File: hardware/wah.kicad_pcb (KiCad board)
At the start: 4 copper layers, 99.1 x 54.5 mm, 34 parts, among them J1 Barrel_Jack_Switch, J2 In, J3 Out, SW1 SW_Push_3PDT, U1 TL072, U2 L78L05_TO92

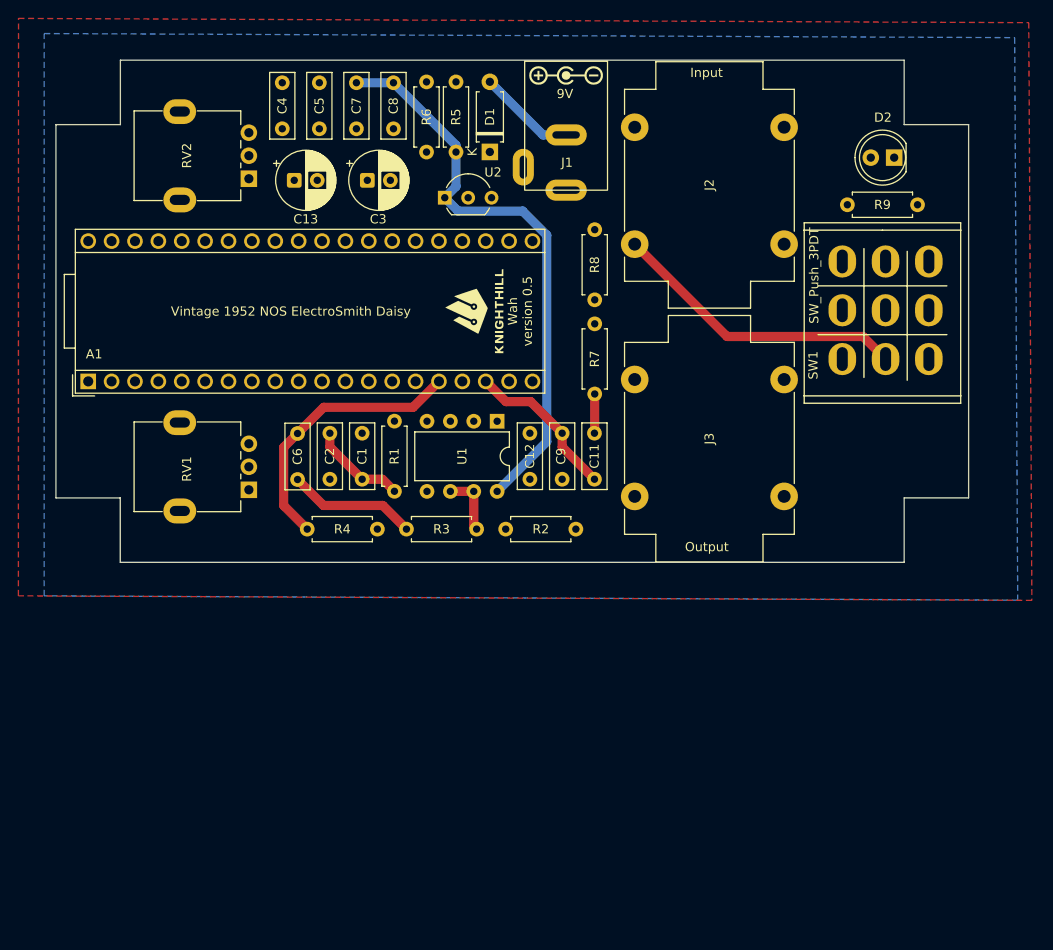
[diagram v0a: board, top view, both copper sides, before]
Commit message: fix footprints
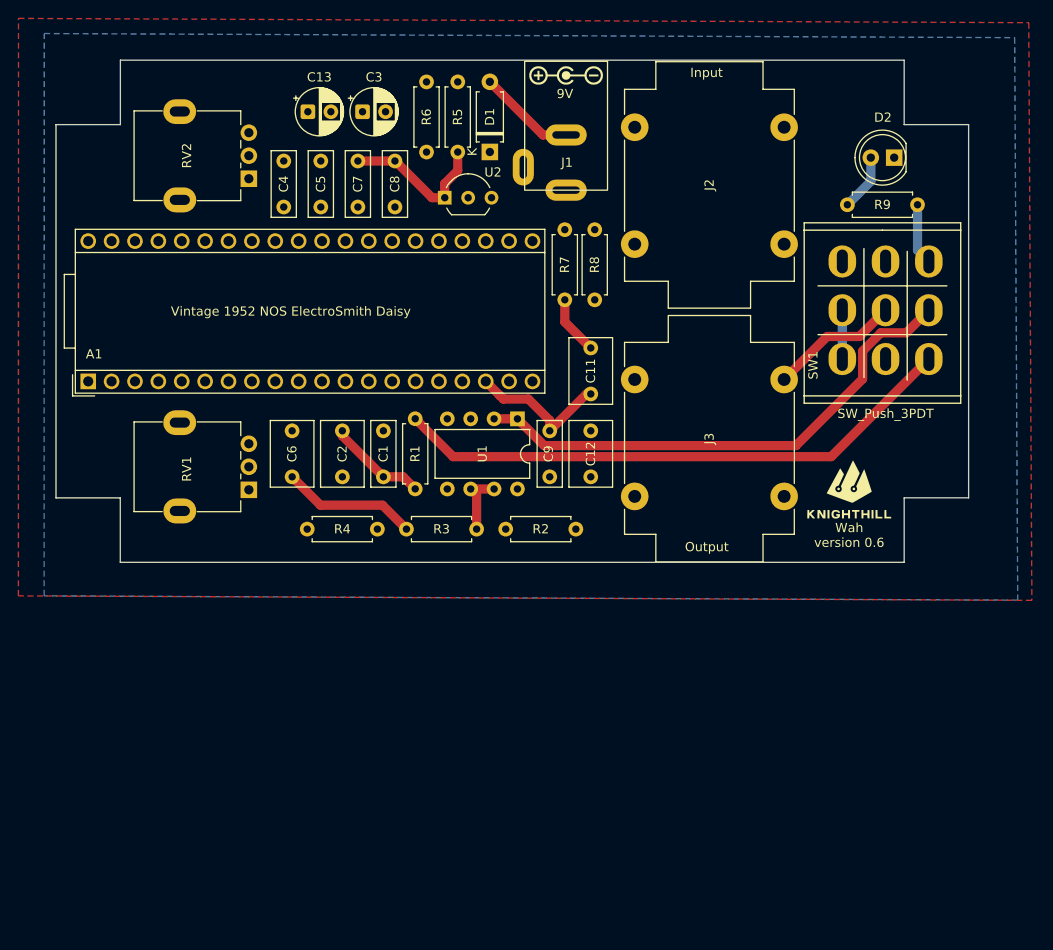
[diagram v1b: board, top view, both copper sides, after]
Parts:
- C11, C12, C2, C6: footprint Capacitor_THT:C_Rect_L7.0mm_W2.5mm_P5.00mm -> Capacitor_THT:C_Rect_L7.0mm_W4.5mm_P5.00mm
- C13, C3: footprint Capacitor_THT:CP_Radial_D6.3mm_P2.50mm -> Capacitor_THT:CP_Radial_D5.0mm_P2.50mm
- moved G*** 44.5 mm to (128.5, 80.7), turned to 0 degrees
- moved R7 10.7 mm to (97.7, 59.2)
- moved C11 9.27 mm to (100.5, 69.4)
- moved C4 8.50 mm to (67.2, 49.1)
- moved C5 8.50 mm to (71.2, 49.1)
- moved C7 8.50 mm to (75.2, 44.1)
- moved C8 8.50 mm to (79.2, 44.1)
- moved C13 7.60 mm to (69.8, 38.8)
- moved C3 7.47 mm to (75.7, 38.8)
- moved C12 6.62 mm to (100.5, 73.4)
- moved C1 2.32 mm to (78.0, 78.4)
- moved R1 2.27 mm to (81.4, 72.1)
- moved U1 2.22 mm to (92.5, 72.1)
- moved C2 1.38 mm to (73.5, 73.4)
- moved C9 1.37 mm to (96.1, 73.4)
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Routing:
- net Net-(U1A-+): track 26.7 -> 39.1 mm
- net Net-(U1C-V+): track 62.7 -> 58.3 mm
- net Net-(U1B-+): track 24.0 -> 21.3 mm
- net /FX_IN: track 64.5 -> 61.9 mm
- net Net-(C11-Pad2): track 4.27 -> 6.40 mm
- net /POT1: track 38.2 -> 36.7 mm
- net /AUDIO_OUT: track 17.1 -> 16.0 mm
- net /AUDIO_IN: track 29.8 -> 30.8 mm
- net Net-(C6-Pad1): track 14.1 -> 14.8 mm
- net /FX_OUT: track 56.9 -> 56.3 mm
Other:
- board text added: "Wah version 0.6"
- board text removed: "Wah version 0.5"

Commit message: rearrange pcb
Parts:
- removed C4, C5: 100n, Capacitor_THT:C_Rect_L7.0mm_W2.5mm_P5.00mm
- moved C7 46.2 mm to (96.4, 85.2), turned to 0 degrees
- moved C8 41.3 mm to (96.4, 81.6), turned to 0 degrees
- moved R2 14.4 mm to (84.6, 85.6)
- moved R3 14.0 mm to (74.2, 85.6)
- moved R1 10.6 mm to (84.6, 82.2), turned to 180 degrees
- moved C13 10.2 mm to (76.5, 46.5)
- moved R4 3.71 mm to (66.5, 82.2)
- moved U1 2.80 mm to (89.8, 71.6)
- moved C1 0.97 mm to (78.4, 77.6)
- moved C2 0.88 mm to (73.7, 72.6)
- moved C6 0.88 mm to (67.9, 77.6)
- moved C3 0.85 mm to (76.5, 39.0)
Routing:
- net Net-(U1B--): track 7.17 -> 15.8 mm
- net Net-(C6-Pad1): track 14.8 -> 9.25 mm
- net Net-(U1B-+): track 21.3 -> 17.7 mm
- net /FX_OUT: track 56.3 -> 59.3 mm
- net Net-(U1A-+): track 39.1 -> 42.1 mm
- net /AUDIO_IN: track 30.8 -> 28.8 mm
- net /FX_IN: track 61.9 -> 60.3 mm
- net Net-(C1-Pad1): track 10.8 -> 12.2 mm
- net /AUDIO_OUT: track 16.0 -> 15.3 mm
- net Net-(U1C-V+): track 58.3 -> 58.9 mm

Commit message: rename resources
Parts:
- renumbered C12 to C10, C7 to C4, C6 to C5, C8 to C6, C13 to C7, C9 to C8, C11 to C9
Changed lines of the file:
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@@
 	(net 38 "Net-(C1-Pad1)")
 	(net 39 "Net-(U1B-+)")
-	(net 40 "Net-(C6-Pad1)")
+	(net 40 "Net-(C5-Pad1)")
 	(net 41 "unconnected-(A1-ADC_3-Pad25)")
 	(net 42 "Net-(U1C-V+)")
-	(net 43 "Net-(C11-Pad2)")
+	(net 43 "Net-(C9-Pad2)")
 	(net 44 "unconnected-(A1-USB_D_--Pad36)")
 	(net 45 "Net-(D1-A)")
@@
 		(descr "C, Rect series, Radial, pin pitch=5.00mm, length*width=7*4.5mm^2, Capacitor")
 		(tags "C Rect series Radial pin pitch 5.00mm length 7mm width 4.5mm Capacitor")
-		(property "Reference" "C11"
+		(property "Reference" "C9"
 			(at 2.5 0 90)
 			(layer "F.SilkS")
@@
 			(layers "*.Cu" "*.Mask")
 			(remove_unused_layers no)
-			(net 43 "Net-(C11-Pad2)")
+			(net 43 "Net-(C9-Pad2)")
 			(pintype "passive")
 		)
@@
 		(descr "C, Rect series, Radial, pin pitch=5.00mm, length*width=7*4.5mm^2, Capacitor")
 		(tags "C Rect series Radial pin pitch 5.00mm length 7mm width 4.5mm Capacitor")
-		(property "Reference" "C6"
+		(property "Reference" "C5"
 			(at 2.5 0 90)
 			(layer "F.SilkS")
@@
 			(layers "*.Cu" "*.Mask")
 			(remove_unused_layers no)
-			(net 40 "Net-(C6-Pad1)")
+			(net 40 "Net-(C5-Pad1)")
 			(pintype "passive")
 		)
@@
 		(descr "CP, Radial series, Radial, pin pitch=2.50mm, diameter=5mm, height=7mm, Electrolytic Capacitor")
 		(tags "CP Radial series Radial pin pitch 2.50mm diameter 5mm height 7mm Electrolytic Capacitor")
-		(property "Reference" "C13"
+		(property "Reference" "C7"
 			(at 1.25 -3.75 0)
 			(layer "F.SilkS")
@@
 		(descr "C, Rect series, Radial, pin pitch=5.00mm, length*width=7*2.5mm^2, Capacitor")
 		(tags "C Rect series Radial pin pitch 5.00mm length 7mm width 2.5mm Capacitor")
-		(property "Reference" "C8"
+		(property "Reference" "C6"
 			(at 2.5 0 0)
 			(layer "F.SilkS")
@@
 			(layers "*.Cu" "*.Mask")
 			(remove_unused_layers no)
-			(net 43 "Net-(C11-Pad2)")
+			(net 43 "Net-(C9-Pad2)")
 			(pintype "passive")
 		)
@@
 			(layers "*.Cu" "*.Mask")
 			(remove_unused_layers no)
-			(net 40 "Net-(C6-Pad1)")
+			(net 40 "Net-(C5-Pad1)")
 			(pintype "passive")
 		)
@@
 		(descr "C, Rect series, Radial, pin pitch=5.00mm, length*width=7*2.5mm^2, Capacitor")
 		(tags "C Rect series Radial pin pitch 5.00mm length 7mm width 2.5mm Capacitor")
-		(property "Reference" "C7"
+		(property "Reference" "C4"
 			(at 2.5 0 0)
 			(layer "F.SilkS")
@@
 		(descr "C, Rect series, Radial, pin pitch=5.00mm, length*width=7*2.5mm^2, Capacitor")
 		(tags "C Rect series Radial pin pitch 5.00mm length 7mm width 2.5mm Capacitor")
-		(property "Reference" "C9"
+		(property "Reference" "C8"
 			(at 2.5 0.125 90)
 			(layer "F.SilkS")
@@
 		(descr "C, Rect series, Radial, pin pitch=5.00mm, length*width=7*4.5mm^2, Capacitor")
 		(tags "C Rect series Radial pin pitch 5.00mm length 7mm width 4.5mm Capacitor")
-		(property "Reference" "C12"
+		(property "Reference" "C10"
 			(at 2.5 0 270)
 			(layer "F.SilkS")

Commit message: pcb
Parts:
- added H1: MountingHole_Pad, MountingHole:MountingHole_3.2mm_M3_Pad, F.Cu at (77.5, 45.9)
- added H2: MountingHole_Pad, MountingHole:MountingHole_3.2mm_M3_Pad, F.Cu at (59.8, 102.8)
- added J4: Conn_01x08_Pin, Connector_PinHeader_2.54mm:PinHeader_1x08_P2.54mm_Vertical, F.Cu at (68.6, 36.0)
- added RV3: 10k, Potentiometer_THT:Potentiometer_Runtron_RM-065_Vertical, F.Cu at (65.5, 92.4)
- added RV4: 10k, Potentiometer_THT:Potentiometer_Runtron_RM-065_Vertical, F.Cu at (56.6, 92.4)
- added SW2: SW_DIP_x04, Button_Switch_THT:SW_DIP_SPSTx04_Slide_9.78x12.34mm_W7.62mm_P2.54mm, F.Cu at (52.6, 87.9)
- RV1, RV2: footprint CustomFootprints:Potentiometer_uxcel_9mm_Single_Vertical -> Potentiometer_THT:Potentiometer_Runtron_RM-065_Vertical
- moved D2 90.3 mm to (78.7, 115.6)
- moved R9 87.0 mm to (72.0, 107.8), turned to -90 degrees
- moved G*** 85.1 mm to (49.4, 112.2)
- moved C3 82.0 mm to (106.4, 115.3)
- moved C7 72.7 mm to (99.9, 115.3)
- moved J3 63.7 mm to (59.6, 53.0), turned to 180 degrees
- moved R8 55.9 mm to (108.8, 107.0), turned to 180 degrees
- moved U2 53.3 mm to (102.5, 98.3)
- moved R5 52.4 mm to (101.2, 93.3), turned to 0 degrees
- moved R6 49.9 mm to (101.2, 89.5), turned to 0 degrees
- moved C9 48.8 mm to (88.8, 116.8), turned to 0 degrees
- moved R7 44.9 mm to (108.8, 102.7), turned to 180 degrees
- moved D1 44.0 mm to (101.2, 85.5), turned to 0 degrees
- moved RV2 38.4 mm to (56.6, 83.8), turned to 90 degrees
- moved C10 38.3 mm to (93.8, 111.2), turned to 180 degrees
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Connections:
- net Net-(J2-PadT) renamed /J_IN
- net Net-(J3-PadT) renamed /J_OUT
- A1 pad 22: unconnected-(A1-ADC_0-Pad22) -> /POT1
- A1 pad 24: /POT1 -> /POT3
- A1 pad 25: unconnected-(A1-ADC_3-Pad25) -> /POT4
- A1 pad 27: unconnected-(A1-ADC_5-Pad27) -> /SW1
- A1 pad 28: unconnected-(A1-ADC_6-Pad28) -> /SW2
- A1 pad 29: unconnected-(A1-DAC_OUT2-Pad29) -> /SW3
- A1 pad 30: unconnected-(A1-DAC_OUT1-Pad30) -> /SW4
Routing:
- net Net-(U1C-V+): track 58.9 -> 0.00 mm
- net Net-(U1A-+): track 42.1 -> 0.00 mm
- net /POT1: track 36.7 -> 0.00 mm
- net /POT2: track 29.6 -> 0.00 mm
- net /AUDIO_IN: track 28.8 -> 0.00 mm
- net /FX_OUT: track 59.3 -> 82.4 mm
- net /FX_IN: track 60.3 -> 78.5 mm
- net Net-(U1B-+): track 17.7 -> 0.00 mm
- net Net-(U1B--): track 15.8 -> 0.00 mm
- net /AUDIO_OUT: track 15.3 -> 0.00 mm
- net Net-(C1-Pad1): track 12.2 -> 0.00 mm
- net Net-(D1-A): track 10.7 -> 0.00 mm
- net /J_OUT: track 14.1 -> 23.9 mm
- net Net-(C5-Pad1): track 9.25 -> 0.00 mm
- net /J_IN: track 32.4 -> 24.8 mm
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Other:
- board size 99.1 x 54.5 mm -> 70 x 87 mm
- board text added: "DryBaby Wah version 0.6"
- board text removed: "Wah version 0.6"

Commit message: pcb changes
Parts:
- removed D2: LED, LED_THT:LED_D5.0mm
- removed R9: R, Resistor_THT:R_Axial_DIN0207_L6.3mm_D2.5mm_P7.62mm_Horizontal
- removed SW1: SW_Push_3PDT, CustomFootprints:Switches_Stomp_Switch_3PDT
- added D3: LED, LED_THT:LED_D5.0mm, F.Cu at (76.2, 41.6)
- added J5: Conn_01x08_Pin, Connector_PinHeader_2.54mm:PinHeader_1x08_P2.54mm_Vertical, F.Cu at (118.7, 93.6)
- added R10: R, Resistor_THT:R_Axial_DIN0207_L6.3mm_D2.5mm_P7.62mm_Horizontal, F.Cu at (83.9, 39.5)
- added SW3: SW_Push_3PDT, CustomFootprints:Switches_Stomp_Switch_3PDT, F.Cu at (131.4, 102.5)
- moved A1 64.2 mm to (108.0, 59.0), turned to -90 degrees
- moved G*** 60.8 mm to (47.7, 57.1)
- moved C7 56.4 mm to (44.6, 104.0)
- moved R8 56.4 mm to (53.5, 95.7)
- moved C3 56.4 mm to (51.1, 104.0)
- moved D1 56.4 mm to (45.9, 74.2)
- moved R6 56.4 mm to (45.9, 78.3)
- moved R7 56.4 mm to (53.5, 91.8)
- moved U2 51.6 mm to (52.3, 86.6), turned to 180 degrees
- moved RV4 49.8 mm to (100.4, 116.2)
- moved R5 48.9 mm to (53.5, 82.2), turned to 180 degrees
- moved J1 46.0 mm to (53.7, 64.3), turned to 0 degrees
- moved RV2 41.8 mm to (83.1, 116.2)
- moved RV3 35.4 mm to (91.7, 116.2)
- moved C9 33.8 mm to (104.1, 86.7), turned to 90 degrees
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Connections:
- J4 pad 7: unconnected-(J4-Pin_7-Pad7) -> /LED
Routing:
- net /FX_OUT: track 82.4 -> 0.00 mm
- net /FX_IN: track 78.5 -> 0.00 mm
- net /J_IN: track 24.8 -> 0.00 mm
- net /J_OUT: track 23.9 -> 0.00 mm
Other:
- board size 70 x 87 mm -> 99.1 x 87 mm
- board text removed: "Vintage 1952 NOS ElectroSmith Daisy"
